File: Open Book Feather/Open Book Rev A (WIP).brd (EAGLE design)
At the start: 77.5 x 112.3 mm, 115 parts, among them J1 SJ-43514-SMT, J2 10118193-0001LF, Q1 DMG341, Q2 IRLML0100, SW1 SPDT_SWITCH, U1 AP2112-3.3, U2 MCP73831T-2ACI/OT, U3 ATSAMD51J64-TQFP(10X10), U4 GD25Q16C (or GD25Q32C), U5 74AC165D, U6 GD25Q16C (or GD25Q32C), U7 23K256-I/SN, X1 JSTPH, X2 2x5 0.05" SWD

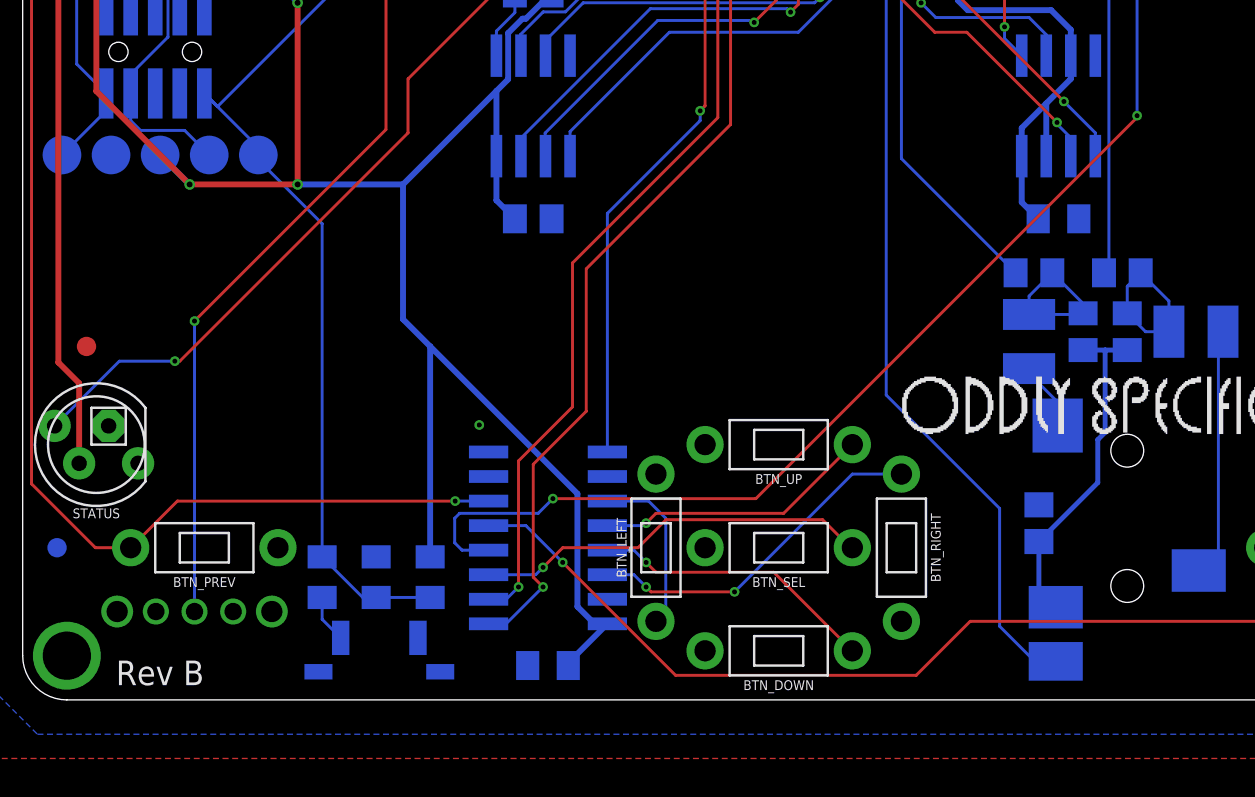
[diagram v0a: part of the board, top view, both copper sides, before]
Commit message: move surface mount chip away from thru-hole components
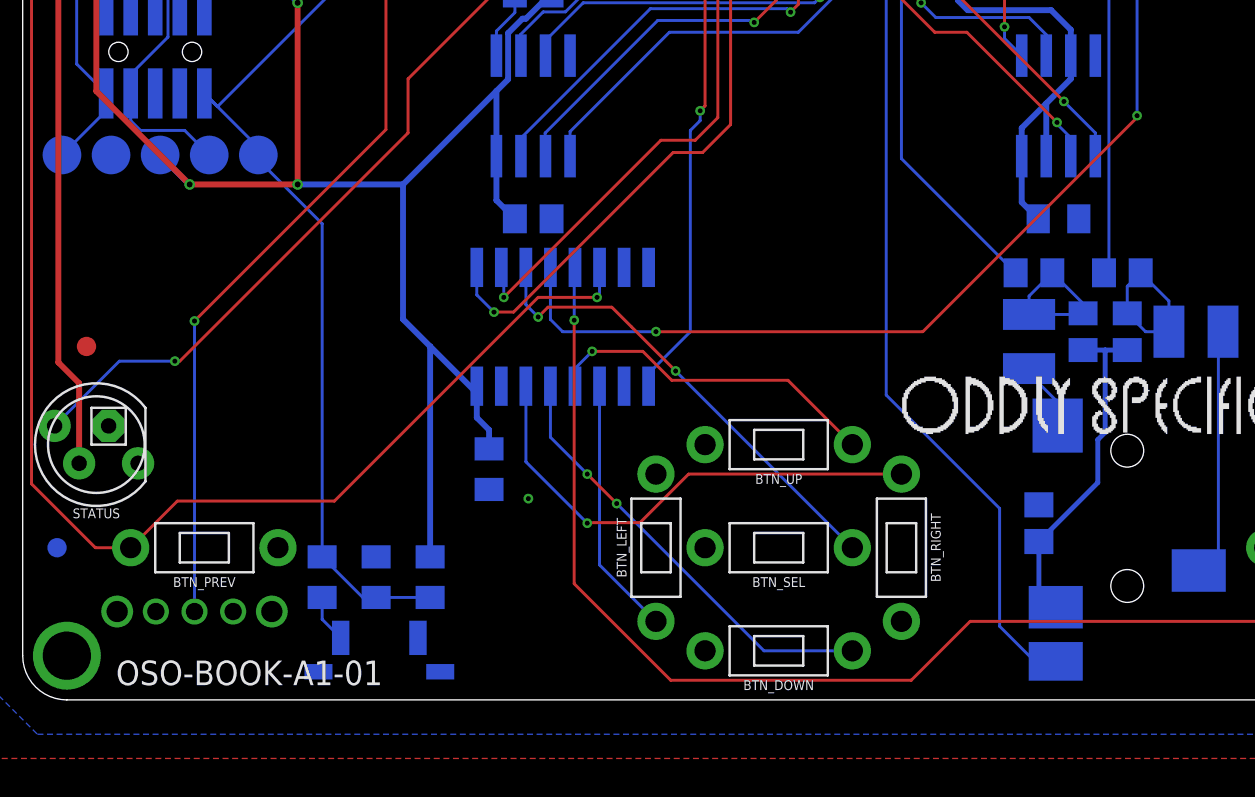
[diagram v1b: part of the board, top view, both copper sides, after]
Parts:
- moved U5 10.9 mm to (27.7, 19.3), turned to 180 degrees
- moved C26 10.6 mm to (23.9, 11.9), turned to 270 degrees
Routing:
- net +3V3: track 448.9 -> 434.3 mm
- net BUTTON_CLK: track 60.3 -> 46.5 mm
- net BUTTON_LATCH: track 62.3 -> 49.2 mm
- net BUTTON7: track 109.0 -> 120.6 mm
- net BUTTON6: track 136.3 -> 147.3 mm
- net BUTTON5: track 194.2 -> 185.0 mm
- net BUTTON2: track 14.8 -> 22.8 mm, vias 1 -> 2
- net BUTTON3: track 18.1 -> 25.7 mm, vias 2 -> 1
- net BUTTON0: track 8.94 -> 13.4 mm
- net BUTTON_OUT: track 49.5 -> 45.2 mm
- net BUTTON4: track 20.6 -> 24.5 mm, vias 1 -> 2
- net BUTTON1: track 14.4 -> 17.6 mm
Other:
- board text added: "...clock D48, data D49 and latch D50."
- board text added: "BUTTONS"
- board text added: "OSO-BOOK-A1-01"
- board text added: "U5 is a 74165 8-bit shift register. It takes the state of the board's 8 buttons (L/D/U/R/Sel/ Prev/Next/Lock) and fits them in a single byte that we can read via..."
- board text removed: "BUTTON REGISTER"
- board text removed: "Note: LOCK is also tied to D51 which can serve as an ext. interrupt"
- board text removed: "Rev B"
- board text removed: "U5 is a fairly generic 74165 8-bit shift register. It takes the state of the board's 8 buttons (Left/Down/Up/Right /Select/Prev/Next/Lock) and fits them in a single byte that we can read with clock D48, data D49 and latch D50."

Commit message: last minute tweaks to text and arrangement
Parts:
- removed MS2: FEATHERWING_SMTDUAL, microbuilder:FEATHERWING_SMT2
- removed U$23: OSO-TEXT-TEST, My Stuff:OSO-TEXT-TEST
- added MS1: FEATHERWING_SMTDUAL, pygamer-microbuilder:FEATHERWING_SMT2
- moved STATUS 1.52 mm to (5.08, 13.2)
- moved C26 1.05 mm to (23.6, 13.0), turned to 180 degrees
- moved R5 0.51 mm to (12.2, 37.3)
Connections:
- net !RESET: now also MS1.1, MS1.1'; no longer MS2.1, MS2.1'
- net +3V3: now also MS1.2, MS1.2'; no longer MS2.2, MS2.2'
- net A0: now also MS1.5, MS1.5'; no longer MS2.5, MS2.5'
- net A1: now also MS1.6, MS1.6'; no longer MS2.6, MS2.6'
- net A2: now also MS1.7, MS1.7'; no longer MS2.7, MS2.7'
- net A3: now also MS1.8, MS1.8'; no longer MS2.8, MS2.8'
- net A4: now also MS1.9, MS1.9'; no longer MS2.9, MS2.9'
- net A5: now also MS1.10, MS1.10'; no longer MS2.10, MS2.10'
- net AVCC: now also MS1.3, MS1.3'; no longer MS2.3, MS2.3'
- net D10: now also MS1.22, MS1.22'; no longer MS2.22, MS2.22'
- net D11: now also MS1.23, MS1.23'; no longer MS2.23, MS2.23'
- net D12: now also MS1.24, MS1.24'; no longer MS2.24, MS2.24'
- net D13: now also MS1.25, MS1.25'; no longer MS2.25, MS2.25'
- net D5: now also MS1.19, MS1.19'; no longer MS2.19, MS2.19'
- net D6: now also MS1.20, MS1.20'; no longer MS2.20, MS2.20'
- net D9: now also MS1.21, MS1.21'; no longer MS2.21, MS2.21'
- net EN: now also MS1.27, MS1.27'; no longer MS2.27, MS2.27'
- net GND: now also MS1.16, MS1.16', MS1.4, MS1.4'; no longer MS2.16, MS2.16', MS2.4, MS2.4'
- net MISO: now also MS1.13, MS1.13'; no longer MS2.13, MS2.13'
- net MOSI: now also MS1.12, MS1.12'; no longer MS2.12, MS2.12'
- net RX: now also MS1.14, MS1.14'; no longer MS2.14, MS2.14'
- net SCK: now also MS1.11, MS1.11'; no longer MS2.11, MS2.11'
- net SCL: now also MS1.18, MS1.18'; no longer MS2.18, MS2.18'
- net SDA: now also MS1.17, MS1.17'; no longer MS2.17, MS2.17'
- net TX: now also MS1.15, MS1.15'; no longer MS2.15, MS2.15'
- net VBAT: now also MS1.28, MS1.28'; no longer MS2.28, MS2.28'
- net VBUS: now also MS1.26, MS1.26'; no longer MS2.26, MS2.26'
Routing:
- net D8_NEOPIX: track 47.8 -> 46.3 mm
- net V+: track 148.3 -> 148.9 mm
- net BUTTON_LATCH: track 49.2 -> 49.7 mm
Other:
- board text added: "...clock D48, data D49 & latch D50. Lock also on D51."
- board text added: "A thru-hole Neopixel (D8) is useful to show CircuitPython status, or you can use it for general blinkenlights."
- board text added: "BUTTON REGISTER"
- board text added: "COLOPHON"
- board text added: "Lots to unpack here. For starters, the Feather header: it's a mostly identical pinout to the Adafruit SAMD51 boards you're familiar with, PWM and analog pins where you expect them (minus the "extra" pin D4). SD and Babel share the main SPI bus. Screen gets its own SPI on SERCOM4 (D41-D43), and also uses: ECS (44), EDC (45), ERST(46), and EBUSY(47). Other peripherals: * status pixel on D8 * button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"
- board text added: "R1 up top pulls EN high. SW1 pulls EN low when switched, disabling 3V power supply U1& most of the board."
- board text added: "R6 pulls reset high. BTN_RESET pulls it low. C13 is a filter cap and R7 limits current spike as C13 discharges."
- board text added: "The Open Book by Joey Castillo @josecastillo. Based in large part on @Adafruit's great open source designs. OSO Logo & lazer bear by Joseph Devens, @DoctorDevens. Thanks to Josh L, Tom F, Brent R. Thanks to 20 years of volunteers behind GNU Unifont: Unifoundry.com. Crafted with . in Brooklyn & Texas."
- board text added: "U4 is another GD25Q16C Flash chip, this tied to the SAMD51's dedicated QSPI bus (D35-D40); it's the CIRCUITPY drive that shows up when you plug it in! R9 pulls U4's CS high; the microcontroller can drive it low (active) via QSPI_CS (D36)."
- board text added: "U5 is a 74165 8-bit shift register. It takes the state of the board's 8 buttons (L/D/U/R/Sel/ Prev/Next/Lock) and fits them in a single byte that we can read via.."
- board text added: "U6 is a GD25Q16C Flash memory chip on the main SPI bus (CS: D52). It stores Unicode character data and Unifont glyphs for every code point in the Basic Multliingual Plane. Contents covered by GPL with font embedding exception."
- board text added: "not a PWM RGB LED! This: https://adafru.it/1938 Data pin at right, power is higher of VBAT and VBUS."
- board text removed: "...clock D48, data D49 and latch D50."
- board text removed: "BUTTONS"
- board text removed: "CREDIT: by Joey Castillo @josecastillo. Based in large part on Adafruit's open source designs. OSO Logo & lazer bear by Joseph Devens @DoctorDevens."
- board text removed: "E-BOOK FEATHER WING"
- board text removed: "Lots to unpack here. For starters, the Feather header: it's a mostly identical pinout to the Adafruit SAMD51 boards you're familiar with, PWM and analog pins where you expect them (minus the "extra" pin D4). SD and Unifont share the main SPI bus. Screen gets its own SPI on SERCOM4 (D41-D43), and also uses: ECS(44) EDC(45) ERST(46) & EBUSY(47). Other peripherals: * status pixel on D8 * buttons on 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"
- board text removed: "R1 up top pulls EN high. This switch connects EN to GND when closed, pulling EN low & disabling regulator U1."
- board text removed: "R6 pulls RESET high. Pressing BTN_RESET pulls it low. C13 is a filter cap and R7 limits any current spike as C13 discharges."
- board text removed: "THANKS TO: Josh L, Tom F, Brent R"
- board text removed: "These are the Feather's UART pins, plus a 3V pin if you need to power something like a GPS. Toss some right angle header on here, it might prove useful."
- board text removed: "U4 is another GD25Q16C Flash chip, this tied to the SAMD51's dedicated QSPI bus (D35-D40); it's the CIRCUITPY drive that shows up when you plug it in! R19 pulls IC2's CS high; the microcontroller can drive it low (active) via QSPI_CS (D36)."
- board text removed: "U5 is a 74165 8-bit shift register. It takes the state of the board's 8 buttons (L/D/U/R/Sel/ Prev/Next/Lock) and fits them in a single byte that we can read via..."
- board text removed: "U6 is a GD25Q16C Flash memory chip. It's on the main SPI bus (CS: D52) and stores glyph bitmaps and Unicode character data for every code point in the Basic Multliingual Plane. Contents covered by GPL with font embedding exception."
- board text removed: "`Previous Page' button (if you want it) ->"
- board text removed: "``Da anni frequento questa biblioteca e la esploro volume per volume, scaffale per scaffale, ma potrei dimostrarvi che non ho fatto altro che portare avanti la lettura d'un unico libro.'' - Italo Calvino, `Se una notte d'inverno un viaggiatore'"
- board text removed: "by joey castillo"

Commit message: yet more last minute text tweaks
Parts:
- moved C26 0.76 mm to (24.4, 13.0)
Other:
- board text added: "C5, C6, C7, C8: filtering caps on each power pin. C11 & C12 filter AVCC, isolated using FB1."
- board text added: "C9&C10: filter"
- board text added: "D1&Q1 conspire to let only the higher of VBAT & VBUS reach 3.3V regulator U1. C1 filters regulator input; C2 & C3 filter output. R1 pulls EN high to keep the regulator on. BATTERY: U2 is a LiPo charging controller. Powered by VBUS, it charges the battery at a rate determined by R3. C4=filter for VBAT, R4 limits current to CHG LED. R14 & R15: a voltage divider for VBAT to make a battery gauge on p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"
- board text added: "caps on VDDCORE, output from the chip's voltage regulator."
- board text removed: "D1&Q1 conspire to let only the higher of VBAT & VBUS reach 3.3V regulator U1. C1 filters regulator input; C2 & C3 filter output. R1 pulls EN high to keep the regulator on. BATTERY: U3 is a LiPo charging controller. Powered by VBUS, it charges the battery at a rate determined by R3. C4=filter for VBAT, R4 limits current to CHG LED, R5&R6 make a voltage divider for VBAT to create voltage monitor on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"
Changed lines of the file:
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@@
 <setting verticaltext="up"/>
 </settings>
-<grid distance="0.01" unitdist="inch" unit="inch" style="lines" multiple="1" display="no" altdistance="0.000123031496" altunitdist="mil" altunit="mil"/>
+<grid distance="0.01" unitdist="inch" unit="mil" style="lines" multiple="1" display="no" altdistance="1" altunitdist="mil" altunit="mil"/>
 <layers>
 <layer number="1" name="Top" color="4" fill="1" visible="yes" active="yes"/>
@@
 <layer number="28" name="bValues" color="7" fill="1" visible="no" active="yes"/>
 <layer number="29" name="tStop" color="7" fill="3" visible="no" active="yes"/>
-<layer number="30" name="bStop" color="7" fill="6" visible="yes" active="yes"/>
+<layer number="30" name="bStop" color="7" fill="6" visible="no" active="yes"/>
 <layer number="31" name="tCream" color="7" fill="4" visible="no" active="yes"/>
 <layer number="32" name="bCream" color="7" fill="5" visible="no" active="yes"/>
@@
 filter output. R1 pulls EN high
 to keep the regulator on.
-BATTERY: U3 is a LiPo charging
+BATTERY: U2 is a LiPo charging
 controller. Powered by VBUS, it
 charges the battery at a rate
 determined by R3. C4=filter for
 VBAT, R4 limits current to CHG
-     LED, R5&amp;R6 make a voltage
-     divider for VBAT to create
-     voltage monitor on pin A6.</text>
+     LED. R14 &amp; R15: a voltage
+     divider for VBAT to make a
+     battery gauge on pin A6.</text>
 <text x="32.004" y="95.758" size="0.508" layer="22" font="vector" ratio="18" rot="MR270" align="center">VBAT</text>
 <text x="45.72" y="105.918" size="0.508" layer="22" font="vector" ratio="18" rot="MR270" align="center">RESET</text>
@@
 <wire x1="21.59" y1="23.622" x2="18.288" y2="26.924" width="0.1524" layer="22" style="shortdash"/>
 <wire x1="6.35" y1="26.924" x2="-0.254" y2="26.924" width="0.1524" layer="22" style="shortdash"/>
+<text x="44.45" y="43.434" size="0.8128" layer="22" font="vector" rot="MR0" align="top-left">C5, C6, C7, C8: filtering
+caps on each power pin.
+C11 &amp; C12 filter AVCC,
+isolated using FB1.</text>
+<text x="33.0454" y="54.102" size="0.8128" layer="22" font="vector" rot="MR90">C9&amp;C10: filter</text>
+<text x="32.6644" y="50.1396" size="0.8128" layer="22" font="vector" rot="MR90" align="top-left">caps on VDDCORE,
+ output from the
+chip's voltage
+regulator.</text>
 </plain>
 <attributes>
@@
 <attribute name="VALUE" x="59.436" y="78.994" size="0.508" layer="28" font="vector" ratio="18" rot="MR90" align="center"/>
 </element>
-<element name="C26" library="microbuilder" package="0805_10MGAP" value="1uF" x="23.622" y="12.954" smashed="yes" rot="MR180">
-<attribute name="NAME" x="23.622" y="11.811" size="0.508" layer="26" font="vector" ratio="18" rot="MR180" align="center"/>
-<attribute name="VALUE" x="25.654" y="13.716" size="0.508" layer="28" font="vector" ratio="18" rot="MR180" align="center"/>
+<element name="C26" library="microbuilder" package="0805_10MGAP" value="1uF" x="24.384" y="12.954" smashed="yes" rot="MR180">
+<attribute name="NAME" x="24.384" y="11.684" size="0.508" layer="26" font="vector" ratio="18" rot="MR180" align="center"/>
+<attribute name="VALUE" x="26.416" y="13.716" size="0.508" layer="28" font="vector" ratio="18" rot="MR180" align="center"/>
 </element>
 <element name="C14" library="microbuilder" package="0805-NO" value="1uF" x="26.162" y="24.892" smashed="yes" rot="MR180">
@@
 <wire x1="52.451" y1="103.124" x2="48.133" y2="103.124" width="0.3048" layer="16"/>
 <wire x1="57.658" y1="103.82" x2="57.216" y2="103.378" width="0.3048" layer="16"/>
-<wire x1="23.241" y1="14.893" x2="22.572" y2="14.224" width="0.3048" layer="16"/>
-<wire x1="22.572" y1="12.954" x2="22.572" y2="14.224" width="0.3048" layer="16"/>
-<wire x1="23.241" y1="14.893" x2="23.241" y2="15.875" width="0.3048" layer="16"/>
+<wire x1="23.241" y1="15.875" x2="23.241" y2="13.047" width="0.3048" layer="16"/>
+<wire x1="23.334" y1="12.954" x2="23.241" y2="13.047" width="0.3048" layer="16"/>
 </signal>
 <signal name="GDR">
@@
 <wire x1="34.20029375" y1="11.684" x2="31.68569375" y2="9.1694" width="0.1524" layer="1"/>
 <wire x1="31.68569375" y1="9.1694" x2="28.9814" y2="9.1694" width="0.1524" layer="1"/>
-<wire x1="28.956" y1="9.144" x2="25.781" y2="12.319" width="0.1524" layer="16"/>
-<wire x1="25.781" y1="12.319" x2="25.781" y2="16.2306" width="0.1524" layer="16"/>
+<wire x1="25.781" y1="16.2306" x2="25.781" y2="14.859" width="0.1524" layer="16"/>
+<wire x1="25.781" y1="14.859" x2="26.416" y2="14.224" width="0.1524" layer="16"/>
+<wire x1="26.416" y1="14.224" x2="26.416" y2="11.684" width="0.1524" layer="16"/>
+<wire x1="26.416" y1="11.684" x2="28.956" y2="9.144" width="0.1524" layer="16"/>
 </signal>
 <signal name="BUTTON4">

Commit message: minor footprint and label tweaks
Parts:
- moved CHG 0.08 mm to (20.6, 110.7)
- moved LED 0.08 mm to (61.2, 110.7)
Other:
- board text added: "CHG"
- board text added: "LED #13"
